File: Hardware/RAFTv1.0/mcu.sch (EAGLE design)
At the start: 2 parts, among them U1 ESP32-D0WD

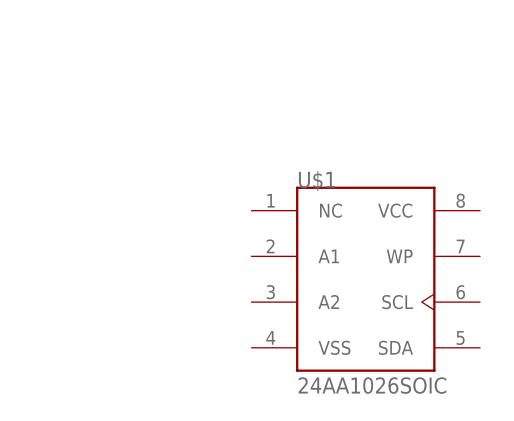
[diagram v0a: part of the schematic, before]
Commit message: changed more libraries. replaced eeprom and flash mem, added datasheets
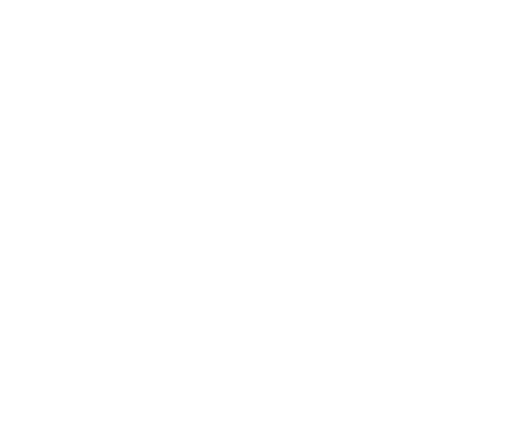
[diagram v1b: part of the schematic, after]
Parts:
- removed U$1: 24AA1026SOIC, 24xx1026SOIC:24AA1026SOIC
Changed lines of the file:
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@@
 <parts>
 <part name="U1" library="ESP32-D0WD" deviceset="ESP32-D0WD" device=""/>
-<part name="U$1" library="24xx1026SOIC" deviceset="24AA1026SOIC" device=""/>
 </parts>
 <sheets>
@@
 <instances>
 <instance part="U1" gate="G$1" x="50.8" y="45.72"/>
-<instance part="U$1" gate="G$1" x="63.5" y="-40.64"/>
 </instances>
 <busses>
